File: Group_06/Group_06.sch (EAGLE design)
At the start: 29 parts, among them J1 POWER_JACKPTH_LOCK, U2 +12v

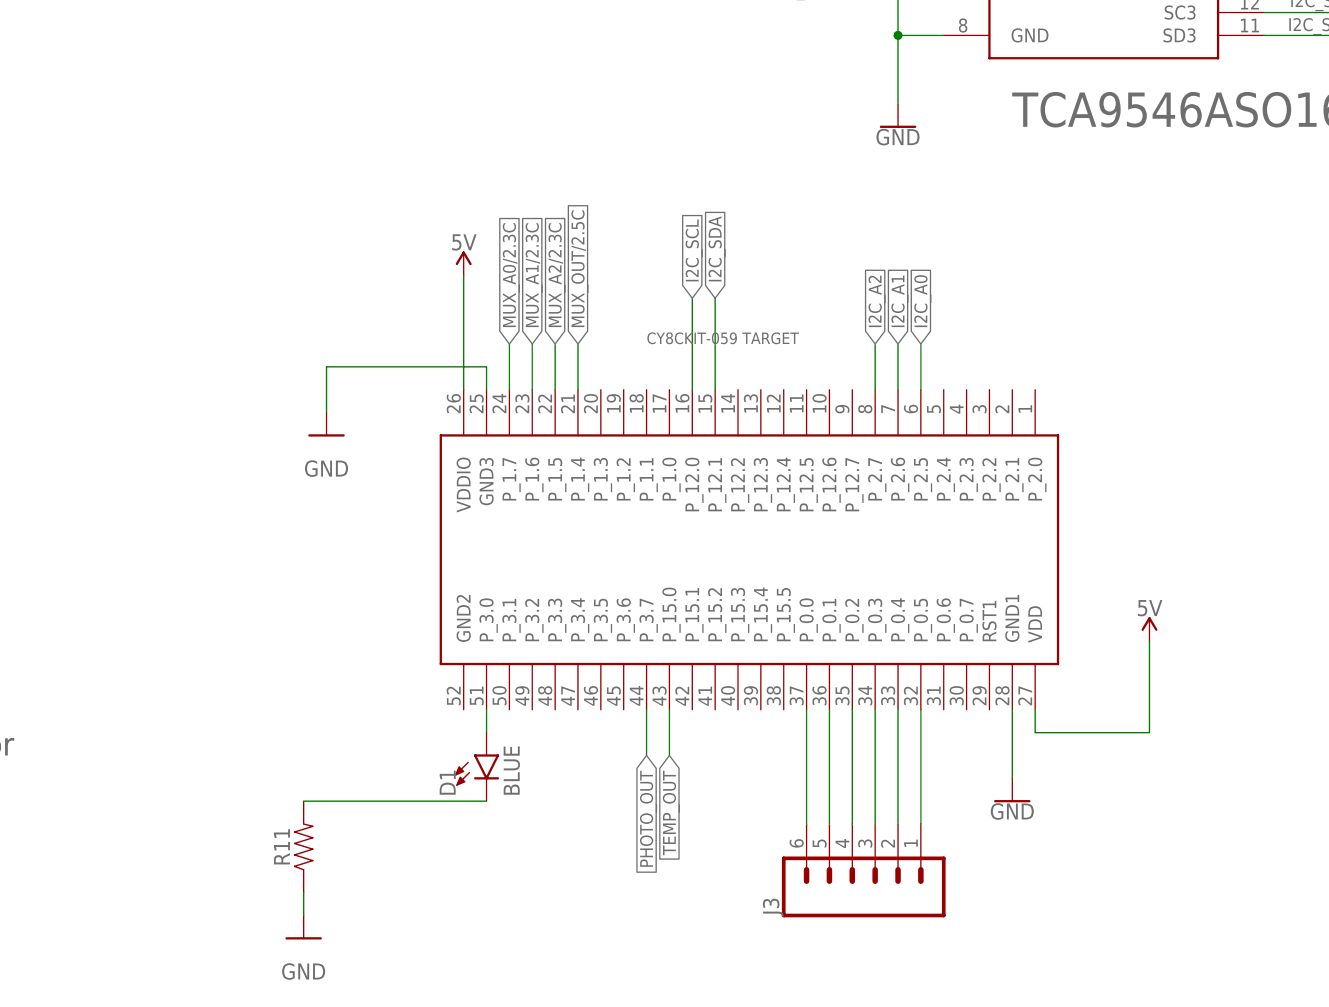
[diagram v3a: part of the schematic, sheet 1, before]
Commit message: Change microcontroller and fixing connection problem
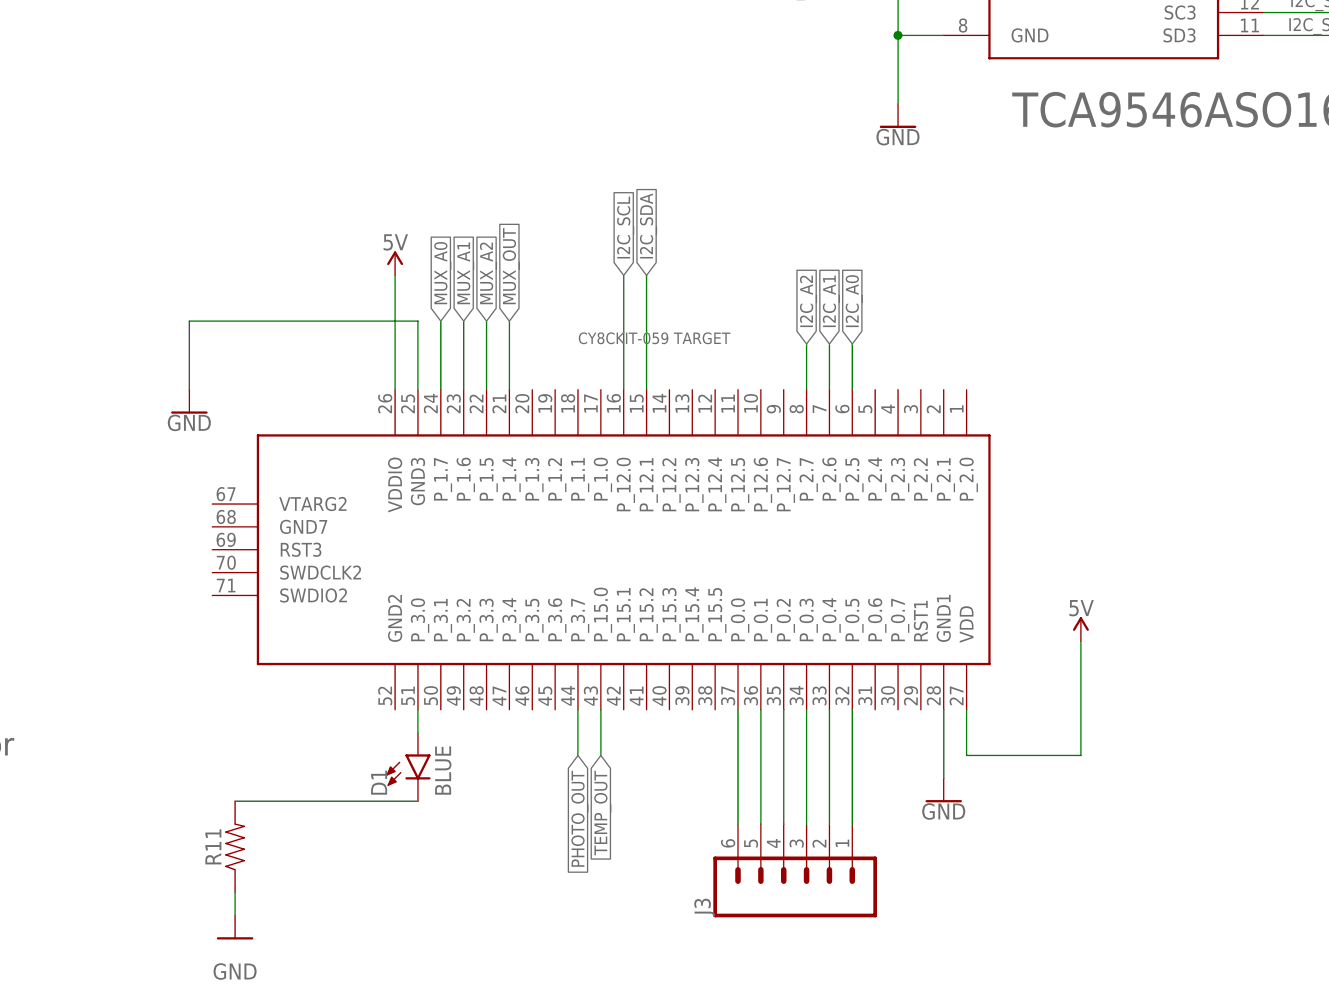
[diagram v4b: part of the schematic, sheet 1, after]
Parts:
- U$2: value CY8CKIT-059_TARGET_3 -> CY8CKIT-059_TARGET; device CY8KIT-059:CY8CKIT-059_TARGET_3 -> CY8KIT-059:CY8CKIT-059_TARGET
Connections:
- removed net MUX_A0/1.3C: U$3.A0
- removed net MUX_A0/2.3C: U$2.P_1.7
- removed net MUX_A1/2.3C: U$2.P_1.6
- removed net MUX_A2/2.3C: U$2.P_1.5
- removed net MUX_OUT/2.5C: U$2.P_1.4
- removed net N$19: U$3.A1
- removed net N$20: U$3.A2
- removed net N$23: U$3.D
- new net MUX_A0: U$2.P_1.7, U$3.A0
- new net MUX_A1: U$2.P_1.6, U$3.A1
- new net MUX_A2: U$2.P_1.5, U$3.A2
- new net MUX_OUT: U$2.P_1.4, U$3.D
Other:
- moved on the sheet: D1, J3, R11

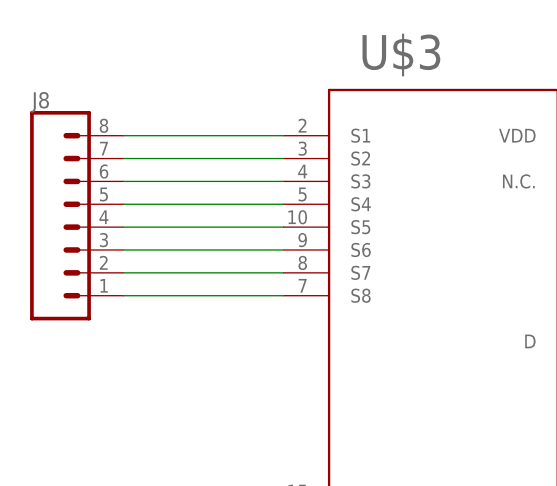
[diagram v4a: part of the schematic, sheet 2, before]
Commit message: Dev corrections (#6)
* Change J8

* Adding component silkscreen
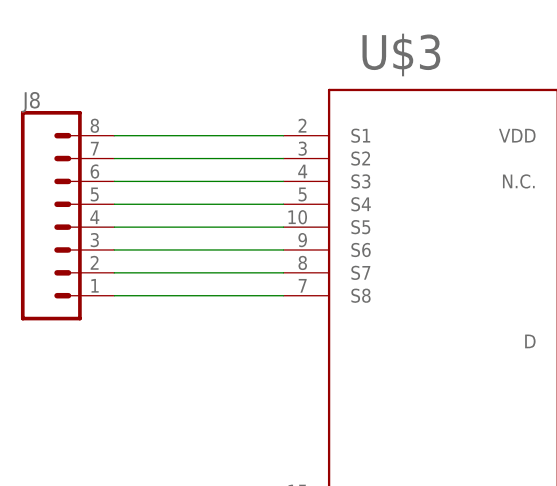
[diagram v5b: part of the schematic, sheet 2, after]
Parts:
- J8: device SparkFun-Connectors:CONN_08" -> SparkFun-Connectors:CONN_08LOCK
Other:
- moved on the sheet: J8
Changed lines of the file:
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@@
 <part name="FRAME2" library="SparkFun-Aesthetics" deviceset="FRAME-A4L" device=""/>
 <part name="U$3" library="Group_06_Library" deviceset="TMUX1208" device="RSV"/>
-<part name="J8" library="SparkFun-Connectors" deviceset="CONN_08" device="&quot;"/>
 <part name="SUPPLY10" library="SparkFun-PowerSymbols" deviceset="5V" device=""/>
 <part name="SUPPLY11" library="SparkFun-PowerSymbols" deviceset="5V" device=""/>
@@
 <part name="J3" library="SparkFun-Connectors" deviceset="CONN_06" device="LOCK"/>
 <part name="U$2" library="CY8KIT-059" deviceset="CY8CKIT-059_TARGET" device=""/>
+<part name="J8" library="SparkFun-Connectors" deviceset="CONN_08" device="LOCK"/>
 </parts>
 <sheets>
@@
 <attribute name="VALUE" x="104.14" y="58.42" size="3.81" layer="95"/>
 </instance>
-<instance part="J8" gate="G$1" x="81.28" y="104.14" smashed="yes">
-<attribute name="VALUE" x="76.2" y="91.694" size="1.778" layer="96" font="vector"/>
-<attribute name="NAME" x="76.2" y="117.348" size="1.778" layer="95" font="vector"/>
-</instance>
 <instance part="SUPPLY10" gate="G$1" x="147.32" y="78.74" smashed="yes">
 <attribute name="VALUE" x="147.32" y="81.534" size="1.778" layer="96" align="bottom-center"/>
@@
 <attribute name="NAME" x="181.864" y="94.361" size="1.778" layer="95" font="vector"/>
 <attribute name="VALUE" x="181.864" y="89.281" size="1.778" layer="96" font="vector"/>
+</instance>
+<instance part="J8" gate="G$1" x="80.264" y="104.14" smashed="yes">
+<attribute name="VALUE" x="75.184" y="91.694" size="1.778" layer="96" font="vector"/>
+<attribute name="NAME" x="75.184" y="117.348" size="1.778" layer="95" font="vector"/>
 </instance>
 </instances>
@@
 </busses>
 <nets>
-<net name="N$10" class="0">
-<segment>
-<pinref part="J8" gate="G$1" pin="8"/>
-<pinref part="U$3" gate="G$1" pin="S1"/>
-<wire x1="86.36" y1="114.3" x2="104.14" y2="114.3" width="0.1524" layer="91"/>
-</segment>
-</net>
-<net name="N$11" class="0">
-<segment>
-<pinref part="J8" gate="G$1" pin="7"/>
-<pinref part="U$3" gate="G$1" pin="S2"/>
-<wire x1="86.36" y1="111.76" x2="104.14" y2="111.76" width="0.1524" layer="91"/>
-</segment>
-</net>
-<net name="N$12" class="0">
-<segment>
-<pinref part="J8" gate="G$1" pin="6"/>
-<pinref part="U$3" gate="G$1" pin="S3"/>
-<wire x1="86.36" y1="109.22" x2="104.14" y2="109.22" width="0.1524" layer="91"/>
-</segment>
-</net>
-<net name="N$13" class="0">
-<segment>
-<pinref part="J8" gate="G$1" pin="5"/>
-<pinref part="U$3" gate="G$1" pin="S4"/>
-<wire x1="86.36" y1="106.68" x2="104.14" y2="106.68" width="0.1524" layer="91"/>
-</segment>
-</net>
-<net name="N$14" class="0">
-<segment>
-<pinref part="J8" gate="G$1" pin="4"/>
-<pinref part="U$3" gate="G$1" pin="S5"/>
-<wire x1="86.36" y1="104.14" x2="104.14" y2="104.14" width="0.1524" layer="91"/>
-</segment>
-</net>
-<net name="N$15" class="0">
-<segment>
-<pinref part="J8" gate="G$1" pin="3"/>
-<pinref part="U$3" gate="G$1" pin="S6"/>
-<wire x1="86.36" y1="101.6" x2="104.14" y2="101.6" width="0.1524" layer="91"/>
-</segment>
-</net>
-<net name="N$16" class="0">
-<segment>
-<pinref part="J8" gate="G$1" pin="2"/>
-<pinref part="U$3" gate="G$1" pin="S7"/>
-<wire x1="86.36" y1="99.06" x2="104.14" y2="99.06" width="0.1524" layer="91"/>
-</segment>
-</net>
-<net name="N$17" class="0">
-<segment>
-<pinref part="J8" gate="G$1" pin="1"/>
-<pinref part="U$3" gate="G$1" pin="S8"/>
-<wire x1="86.36" y1="96.52" x2="104.14" y2="96.52" width="0.1524" layer="91"/>
-</segment>
-</net>
 <net name="GND" class="0">
 <segment>
@@
 </segment>
 </net>
+<net name="N$2" class="0">
+<segment>
+<pinref part="U$3" gate="G$1" pin="S1"/>
+<pinref part="J8" gate="G$1" pin="8"/>
+<wire x1="104.14" y1="114.3" x2="85.344" y2="114.3" width="0.1524" layer="91"/>
+</segment>
+</net>
+<net name="N$10" class="0">
+<segment>
+<pinref part="U$3" gate="G$1" pin="S2"/>
+<pinref part="J8" gate="G$1" pin="7"/>
+<wire x1="104.14" y1="111.76" x2="85.344" y2="111.76" width="0.1524" layer="91"/>
+</segment>
+</net>
+<net name="N$11" class="0">
+<segment>
+<pinref part="U$3" gate="G$1" pin="S3"/>
+<pinref part="J8" gate="G$1" pin="6"/>
+<wire x1="104.14" y1="109.22" x2="85.344" y2="109.22" width="0.1524" layer="91"/>
+</segment>
+</net>
+<net name="N$12" class="0">
+<segment>
+<pinref part="U$3" gate="G$1" pin="S4"/>
+<pinref part="J8" gate="G$1" pin="5"/>
+<wire x1="104.14" y1="106.68" x2="85.344" y2="106.68" width="0.1524" layer="91"/>
+</segment>
+</net>
+<net name="N$13" class="0">
+<segment>
+<pinref part="U$3" gate="G$1" pin="S5"/>
+<pinref part="J8" gate="G$1" pin="4"/>
+<wire x1="104.14" y1="104.14" x2="85.344" y2="104.14" width="0.1524" layer="91"/>
+</segment>
+</net>
+<net name="N$14" class="0">
+<segment>
+<pinref part="U$3" gate="G$1" pin="S6"/>
+<pinref part="J8" gate="G$1" pin="3"/>
+<wire x1="104.14" y1="101.6" x2="85.344" y2="101.6" width="0.1524" layer="91"/>
+</segment>
+</net>
+<net name="N$15" class="0">
+<segment>
+<pinref part="U$3" gate="G$1" pin="S7"/>
+<pinref part="J8" gate="G$1" pin="2"/>
+<wire x1="104.14" y1="99.06" x2="85.344" y2="99.06" width="0.1524" layer="91"/>
+</segment>
+</net>
+<net name="N$16" class="0">
+<segment>
+<pinref part="U$3" gate="G$1" pin="S8"/>
+<pinref part="J8" gate="G$1" pin="1"/>
+<wire x1="104.14" y1="96.52" x2="85.344" y2="96.52" width="0.1524" layer="91"/>
+</segment>
+</net>
